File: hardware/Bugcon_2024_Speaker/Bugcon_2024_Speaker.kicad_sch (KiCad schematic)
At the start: 47 parts, among them J1 OLED, J2 Add_On, J4 Battery, J5 Battery, P1 USB_C_Plug_USB2.0, Q1 DMG3415U-7, SW1 ON, U1 ESP32-C6-WROOM-1U-N4, U2 AP2112K-3.3

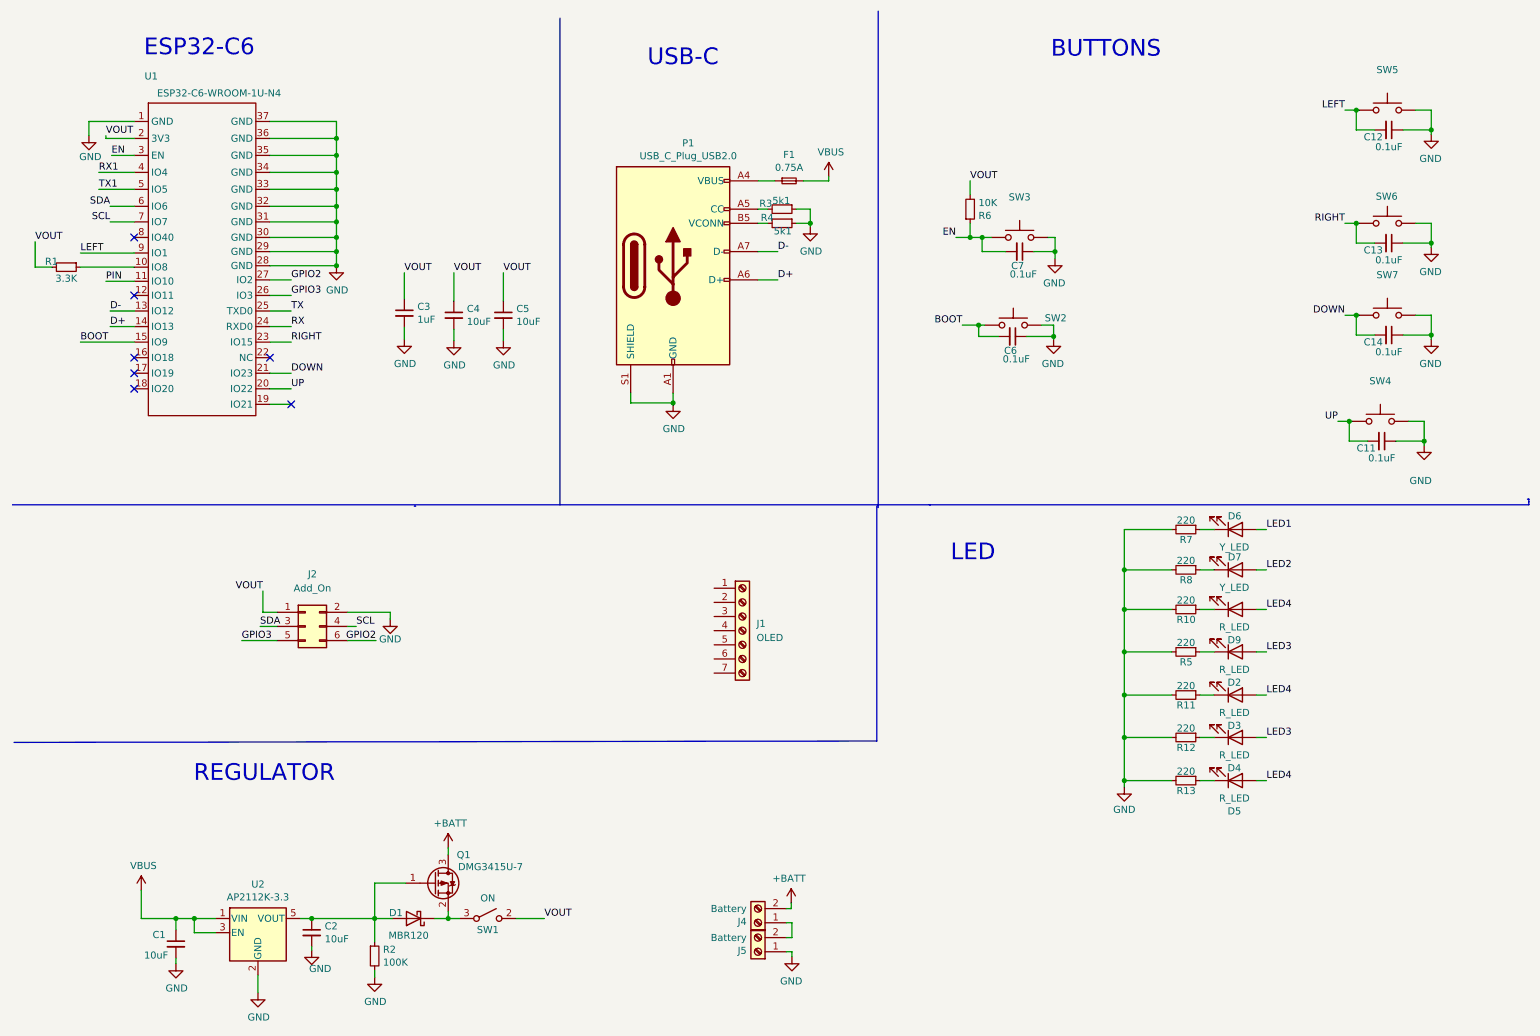
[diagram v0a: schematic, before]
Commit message: feat(Hw): Update route
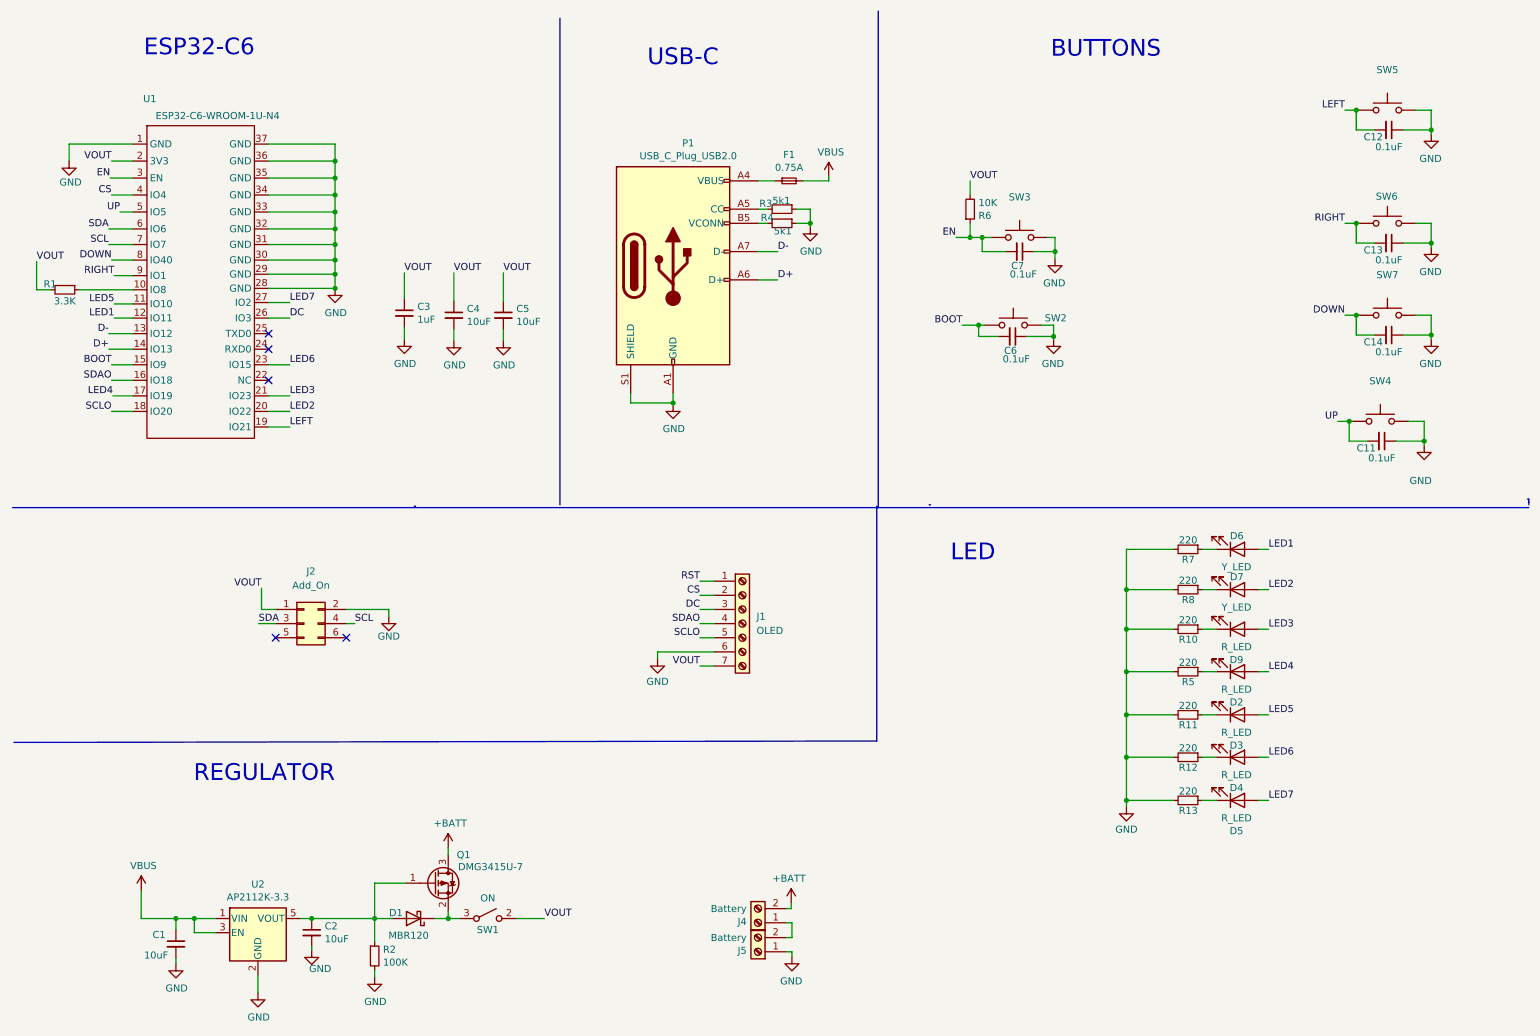
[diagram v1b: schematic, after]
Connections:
- net RX1 is gone; now on net CS: U1.4 (IO4)
- net TX1 is gone; now on net UP: U1.5 (IO5)
- net DOWN: now also U1.8 (IO40); no longer U1.21 (IO23)
- net GND: now also J1.6 (Pin_6)
- net LED1: now also U1.12 (IO11)
- net LED2: now also U1.20 (IO22)
- net LED3: now also D9.2 (A), U1.21 (IO23); no longer D2.2 (A), D4.2 (A)
- net LED4: now also D2.2 (A), U1.17 (IO19); no longer D3.2 (A), D5.2 (A), D9.2 (A)
- net LEFT: now also U1.19 (IO21); no longer U1.9 (IO1)
- net RIGHT: now also U1.9 (IO1); no longer U1.23 (IO15)
- net UP: no longer U1.20 (IO22)
- net VOUT: now also J1.7 (Pin_7)
- net SDAO: now reaches U1.16 (IO18)
- net SDAO: now also J1.4 (Pin_4)
- net SCLO: now reaches U1.18 (IO20)
- net SCLO: now also J1.5 (Pin_5)
- net RST: now reaches J1.1 (Pin_1)
- net CS: now reaches J1.2 (Pin_2)
- net DC: now reaches J1.3 (Pin_3)
- net DC: now also U1.26 (IO3)
- net GPIO2: no longer names the net of J2.6 (Pin_6)
- net GPIO2: no longer U1.27 (IO2)
- net GPIO3: no longer names the net of J2.5 (Pin_5)
- net GPIO3: no longer U1.26 (IO3)
- net PIN renamed LED5
- net LED5: now also D3.2 (A)
- net RX: no longer names the net of U1.24 (RXD0)
- net TX: no longer names the net of U1.25 (TXD0)
- new net LED6: D4.2 (A), U1.23 (IO15)
- new net LED7: D5.2 (A), U1.27 (IO2)
- no-connect marks 7 -> 5
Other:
- moved on the sheet: D2, D3, D4, D5, D6, D7, D9, J1, J2, R1, R10, R11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

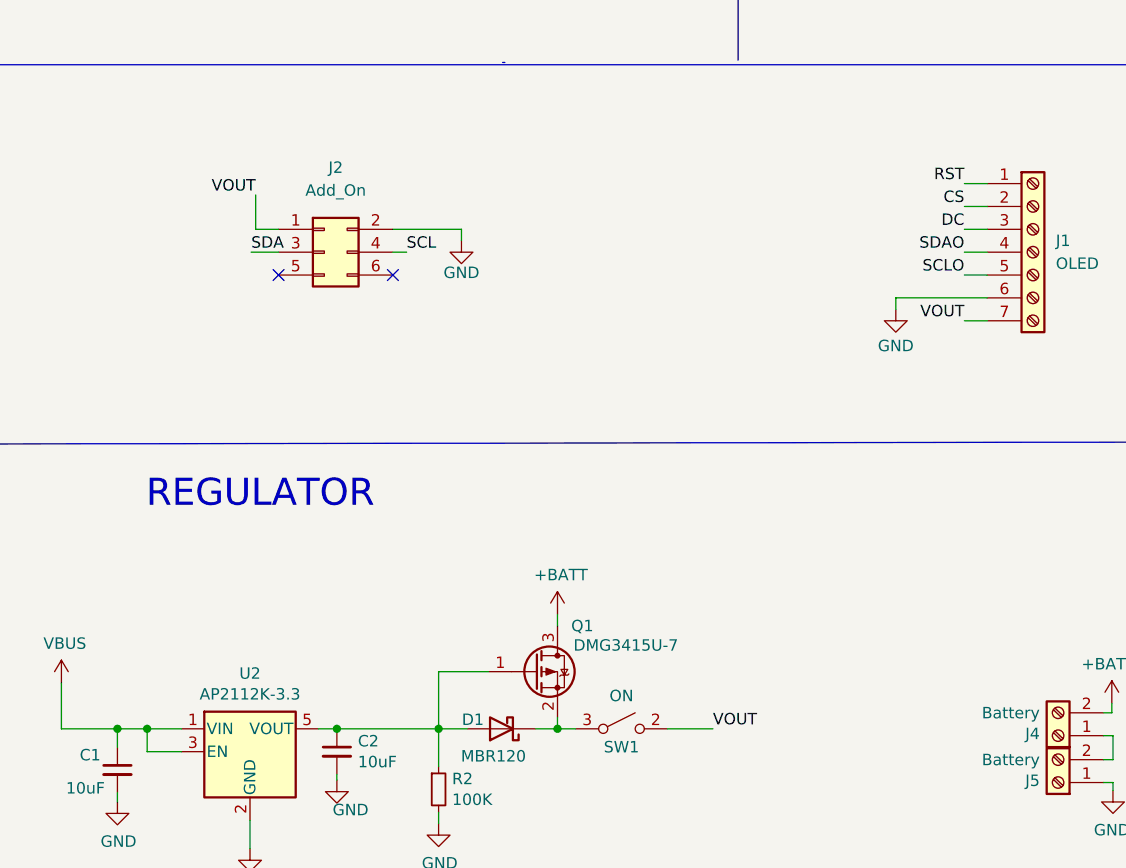
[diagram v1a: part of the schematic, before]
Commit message: feat(Hw):Connected_Reset_Update_Regulator
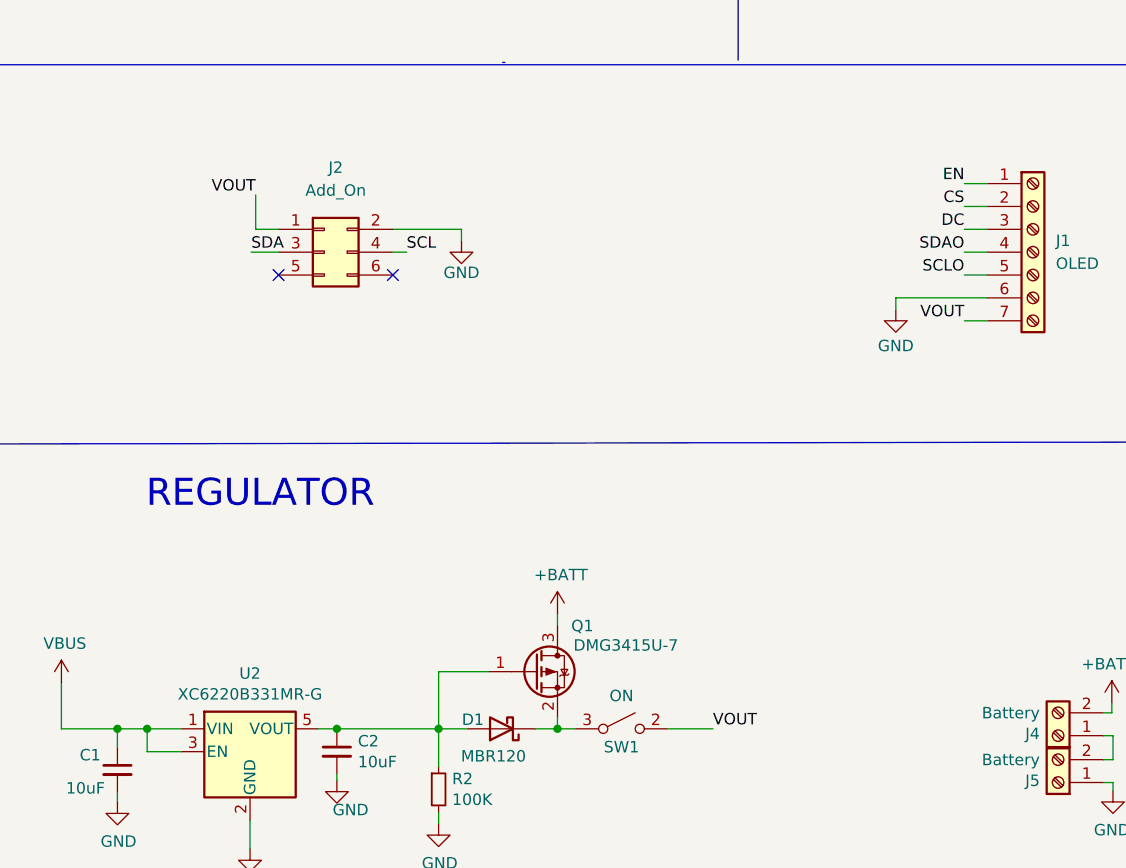
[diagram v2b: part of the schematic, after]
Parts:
- U2: value AP2112K-3.3 -> XC6220B331MR-G; LCSC# C51118 -> C86534; manf# AP2112K3.3TRG -> XC6220B331MR-G
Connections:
- net RST is gone; now on net EN: J1.1 (Pin_1)
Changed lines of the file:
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@@
 		)
 	)
+	(label "EN"
+		(at 135.89 114.3 180)
+		(fields_autoplaced yes)
+		(effects
+			(font
+				(size 1.27 1.27)
+			)
+			(justify right bottom)
+		)
+	)
 	(label "CS"
 		(at 30.226 44.958 180)
@@
 		)
 	)
-	(label "RST"
-		(at 135.89 114.3 180)
-		(fields_autoplaced yes)
-		(effects
-			(font
-				(size 1.27 1.27)
-			)
-			(justify right bottom)
-		)
-	)
 	(label "DC"
 		(at 62.23 67.056 0)
@@
 			)
 		)
-		(property "Value" "AP2112K-3.3"
+		(property "Value" "XC6220B331MR-G"
 			(at 56.515 171.0436 0)
 			(effects
@@
 			)
 		)
-		(property "manf#" "AP2112K3.3TRG"
+		(property "manf#" "XC6220B331MR-G "
 			(at 56.515 177.419 0)
 			(effects
@@
 			)
 		)
-		(property "LCSC#" "C51118"
+		(property "LCSC#" "C86534"
 			(at 56.515 177.419 0)
 			(effects

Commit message: feat(Hw): Update ground areas
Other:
- company: (none) -> Electronic Cats
- title: (none) -> Bugcon_2024_Speaker
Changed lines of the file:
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@@
 	(generator_version "8.0")
 	(paper "A4")
+	(title_block
+		(title "Bugcon_2024_Speaker")
+		(date "2024-09-05")
+		(rev "v1.0")
+		(company "Electronic Cats")
+		(comment 1 "Lizeth Gallegos Martínez")
+	)
 	(junction
 		(at 212.471 138.303)

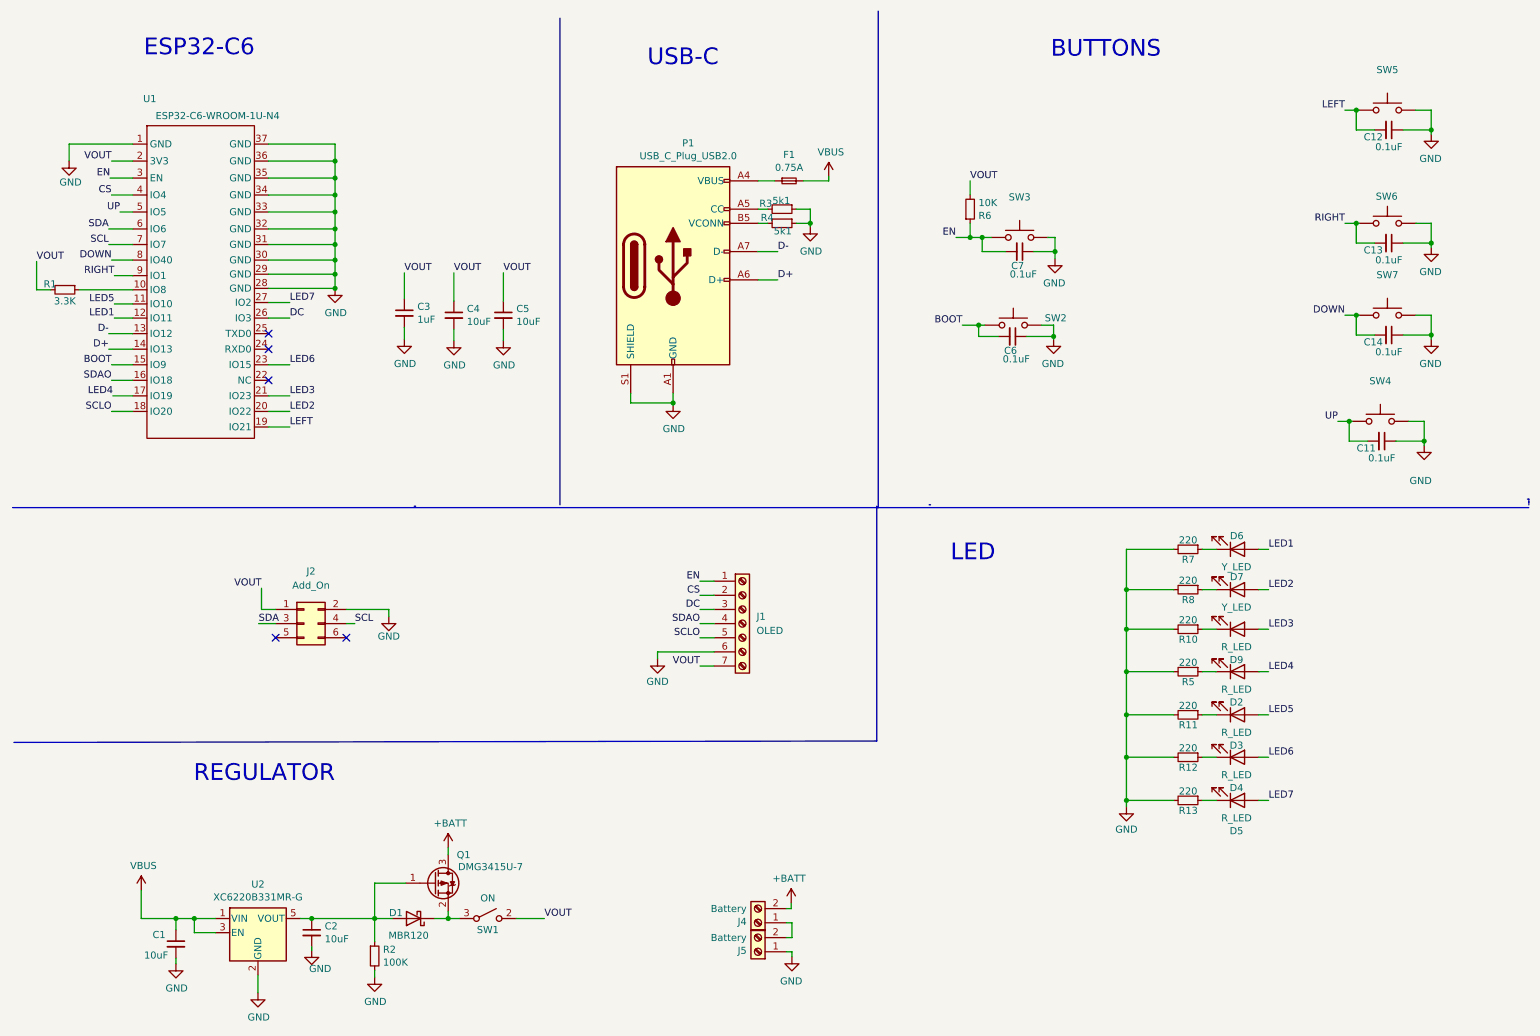
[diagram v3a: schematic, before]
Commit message: feat(Hw): Change LEDs
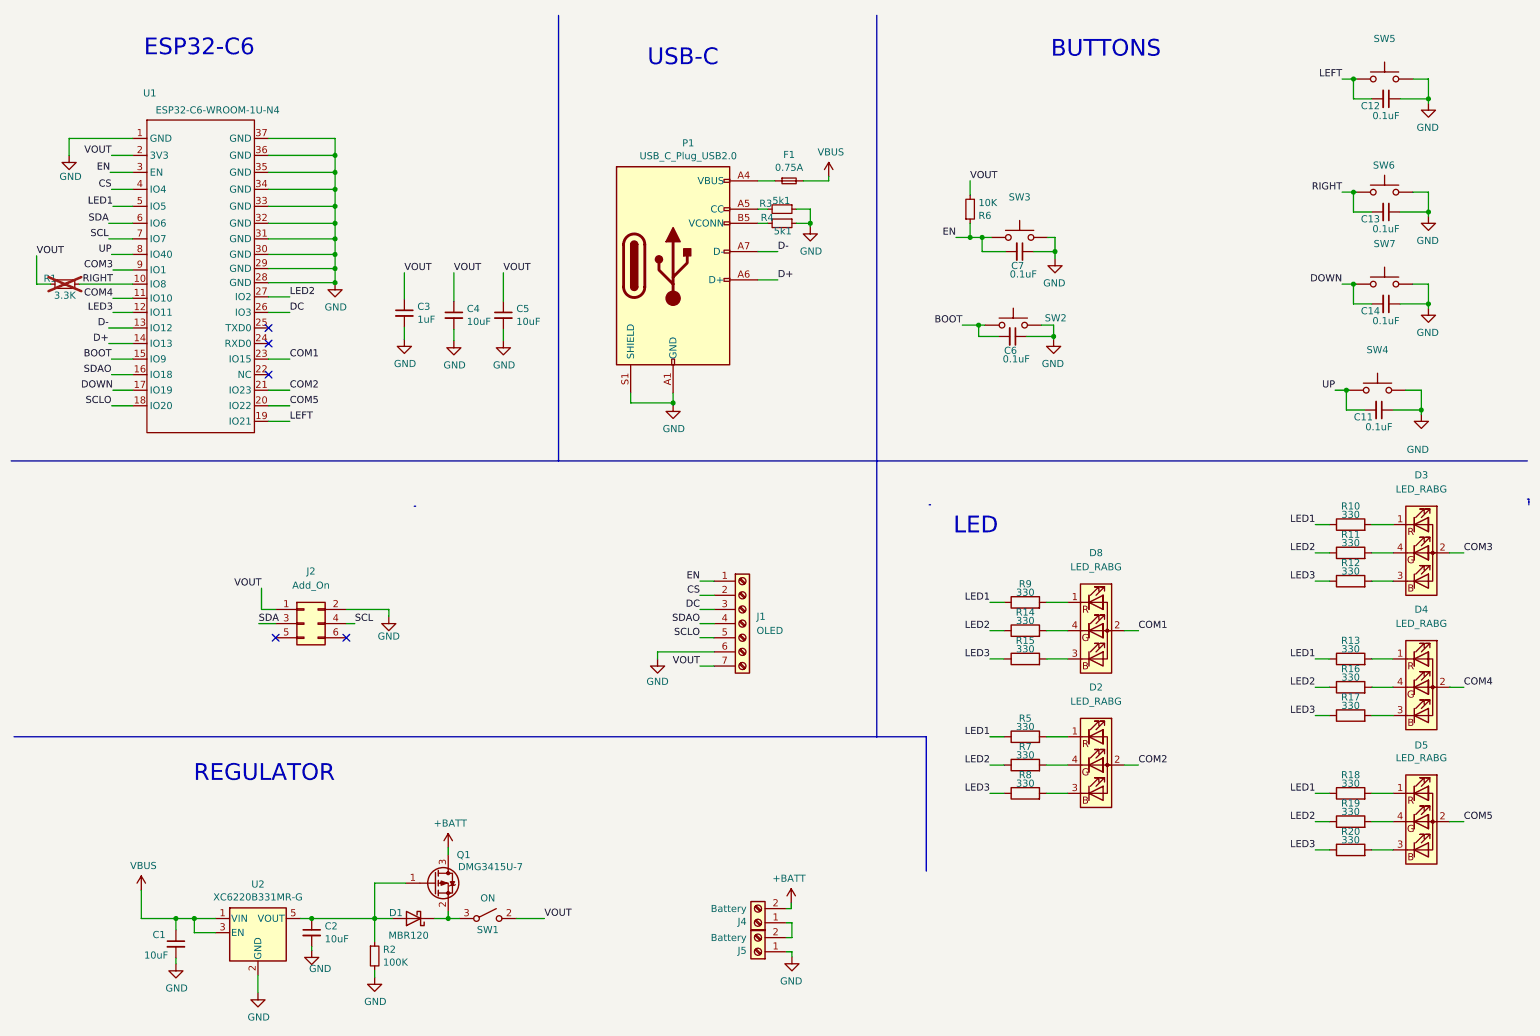
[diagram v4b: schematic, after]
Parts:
- removed D2, D3, D4, D5, D9: R_LED, Library:LYT77K-K2M1, symbol Device:LED
- removed D6, D7: Y_LED, Library:LYT77K-K2M1, symbol Device:LED
- removed R10, R11, R12, R13, R5, R7, R8: 220, Resistor_SMD:R_0603_1608Metric_Pad0.98x0.95mm_HandSolder, symbol Device:R_Small
- added D2, D3, D4, D5, D8: LED_RABG, Library:AAA3528SURKCGKC09, symbol Device:LED_RABG
- added R10, R11, R12, R13, R14, R15, R16, R17, R18, R19, R20, R5, R7, R8, R9: 330, Resistor_SMD:R_0603_1608Metric, symbol Device:R
- R1: now not fitted
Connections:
- net LED4 is gone; now on net DOWN: U1.17 (IO19)
- net LED7 is gone; now on net LED2: U1.27 (IO2)
- net DOWN: no longer U1.8 (IO40)
- net LED1: now also U1.5 (IO5), R10.1, R13.1, R18.1, R5.1, R9.1; no longer U1.12 (IO11)
- net LED2: now also R11.1, R14.1, R16.1, R19.1, R7.1; no longer U1.20 (IO22)
- net LED3: now also U1.12 (IO11), R12.1, R15.1, R17.1, R20.1, R8.1; no longer U1.21 (IO23)
- net RIGHT: now also R1.1, U1.10 (IO8); no longer U1.9 (IO1)
- net UP: now also U1.8 (IO40); no longer U1.5 (IO5)
- net LED5 renamed COM4
- net COM4: now also D4.2 (A)
- net LED6 renamed COM1
- net COM1: now also D8.2 (A)
- new net: D2.1 (RK), R5.2
- new net: D8.1 (RK), R9.2
- new net: D8.3 (BK), R15.2
- new net: D8.4 (GK), R14.2
- new net: D4.1 (RK), R13.2
- new net: D4.3 (BK), R17.2
- new net: D4.4 (GK), R16.2
- new net: D3.4 (GK), R11.2
- new net: D3.1 (RK), R10.2
- new net: D3.3 (BK), R12.2
- new net: D5.3 (BK), R20.2
- new net: D5.4 (GK), R19.2
- new net: D2.3 (BK), R8.2
- new net: D2.4 (GK), R7.2
- new net: D5.1 (RK), R18.2
- new net COM2: D2.2 (A), U1.21 (IO23)
- new net COM3: D3.2 (A), U1.9 (IO1)
- new net COM5: D5.2 (A), U1.20 (IO22)
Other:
- moved on the sheet: C11, C12, C13, C14, SW4, SW5, SW6, SW7, U1

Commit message: fix(hw): fix pins for OLED
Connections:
- net DOWN: no longer U1.17 (IO19)
- net EN: no longer J1.1 (Pin_1)
- net LEFT: no longer U1.19 (IO21)
- net SCLO: no longer U1.18 (IO20)
- net SDAO: now also U1.17 (IO19); no longer U1.16 (IO18)
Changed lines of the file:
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@@
 	)
 	(label "LEFT"
-		(at 62.23 85.598 0)
-		(fields_autoplaced yes)
-		(effects
-			(font
-				(size 1.27 1.27)
-			)
-			(justify left bottom)
+		(at 30.48 82.55 180)
+		(fields_autoplaced yes)
+		(effects
+			(font
+				(size 1.27 1.27)
+			)
+			(justify right bottom)
 		)
 	)
@@
 	)
 	(label "SDAO"
-		(at 30.226 77.216 180)
+		(at 30.48 80.01 180)
 		(fields_autoplaced yes)
 		(effects
@@
 		)
 	)
-	(label "EN"
-		(at 135.89 114.3 180)
-		(fields_autoplaced yes)
-		(effects
-			(font
-				(size 1.27 1.27)
-			)
-			(justify right bottom)
-		)
-	)
 	(label "COM4"
 		(at 273.05 133.35 0)
@@
 	)
 	(label "SCLO"
-		(at 30.226 82.804 180)
-		(fields_autoplaced yes)
-		(effects
-			(font
-				(size 1.27 1.27)
-				(color 184 30 255 1)
-			)
-			(justify right bottom)
+		(at 62.23 85.09 0)
+		(fields_autoplaced yes)
+		(effects
+			(font
+				(size 1.27 1.27)
+				(color 184 30 255 1)
+			)
+			(justify left bottom)
 		)
 	)
@@
 	)
 	(label "DOWN"
-		(at 30.48 80.01 180)
-		(fields_autoplaced yes)
-		(effects
+		(at 30.48 77.47 180)
+		(fields_autoplaced yes)
+		(effects
